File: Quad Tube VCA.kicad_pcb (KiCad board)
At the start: 2 copper layers, 162.6 x 100.3 mm, 226 parts, among them IC1 TL072, IC10 TL072, IC2 LM358, IC3 TL072, IC4 LM358, IC5 TL072, IC6 LM358, IC7 TL072, IC8 LM358, IC9 TL072

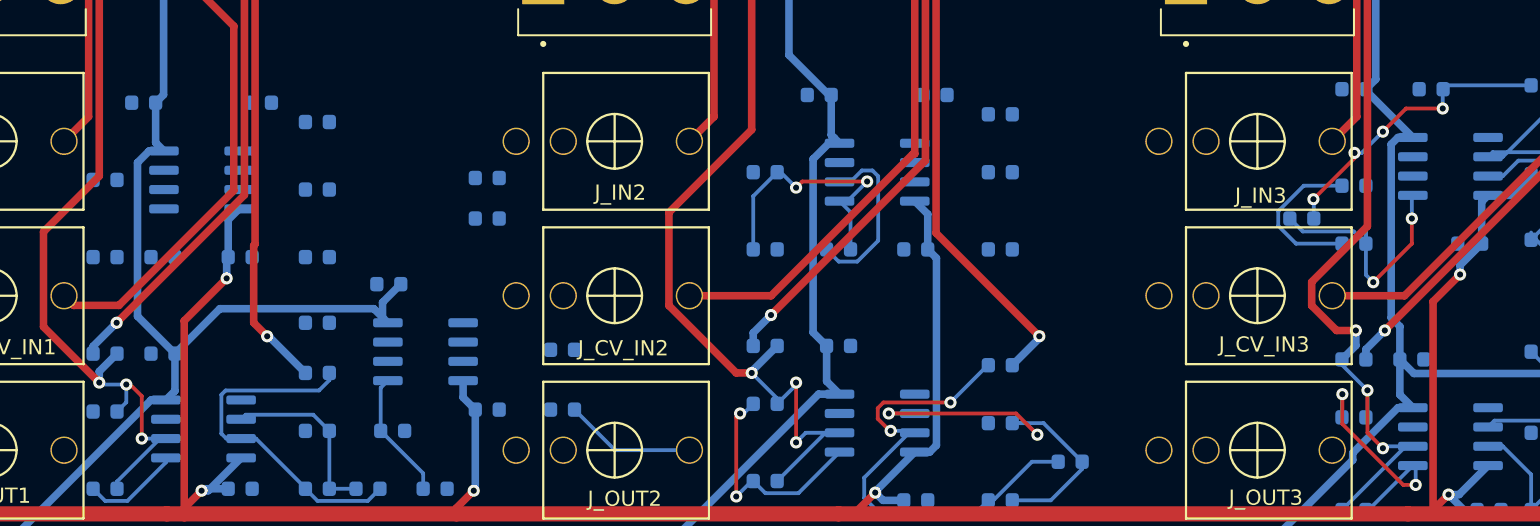
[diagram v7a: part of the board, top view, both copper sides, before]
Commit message: op amp traces [WIP]
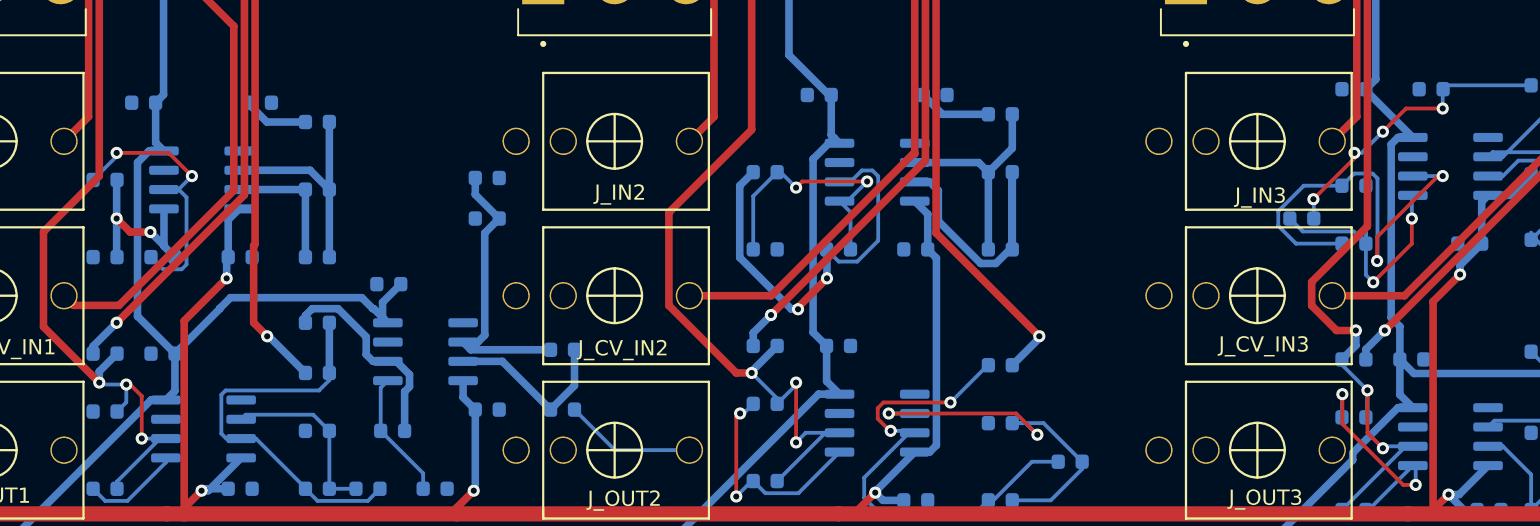
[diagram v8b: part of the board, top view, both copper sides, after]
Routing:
- net Net-(C20-Pad2): track 0.00 -> 20.3 mm
- net Net-(C9-Pad1): track 0.00 -> 19.1 mm, vias 0 -> 2
- net Net-(IC9-Pad6): track 0.00 -> 19.0 mm
- net Net-(C33-Pad1): track 10.5 -> 28.3 mm, vias 0 -> 2
- net Net-(C21-Pad1): track 11.5 -> 27.5 mm, vias 0 -> 2
- net Net-(C8-Pad1): track 0.00 -> 15.3 mm
- net Net-(C20-Pad1): track 0.00 -> 14.6 mm
- net Net-(IC9-Pad2): track 0.00 -> 13.8 mm
- net Net-(C9-Pad2): track 0.00 -> 12.5 mm, vias 0 -> 2
- net Net-(IC9-Pad7): track 0.00 -> 11.7 mm
- net Net-(C8-Pad2): track 0.00 -> 8.80 mm
- net Net-(C26-Pad1): track 0.00 -> 4.82 mm
- net Net-(C14-Pad1): track 0.00 -> 4.34 mm
- net Net-(C4-Pad2): track 23.2 -> 26.5 mm
- net -12V: track 593.1 -> 593.7 mm
